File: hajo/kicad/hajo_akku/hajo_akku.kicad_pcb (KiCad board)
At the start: 2 copper layers, 62 x 92 mm, 21 parts, among them J1 Seetalk NG, J2 Debug, J3 Batteries, U1 MCP2562, U2 LF50CV, U3 WeMos_S2_mini

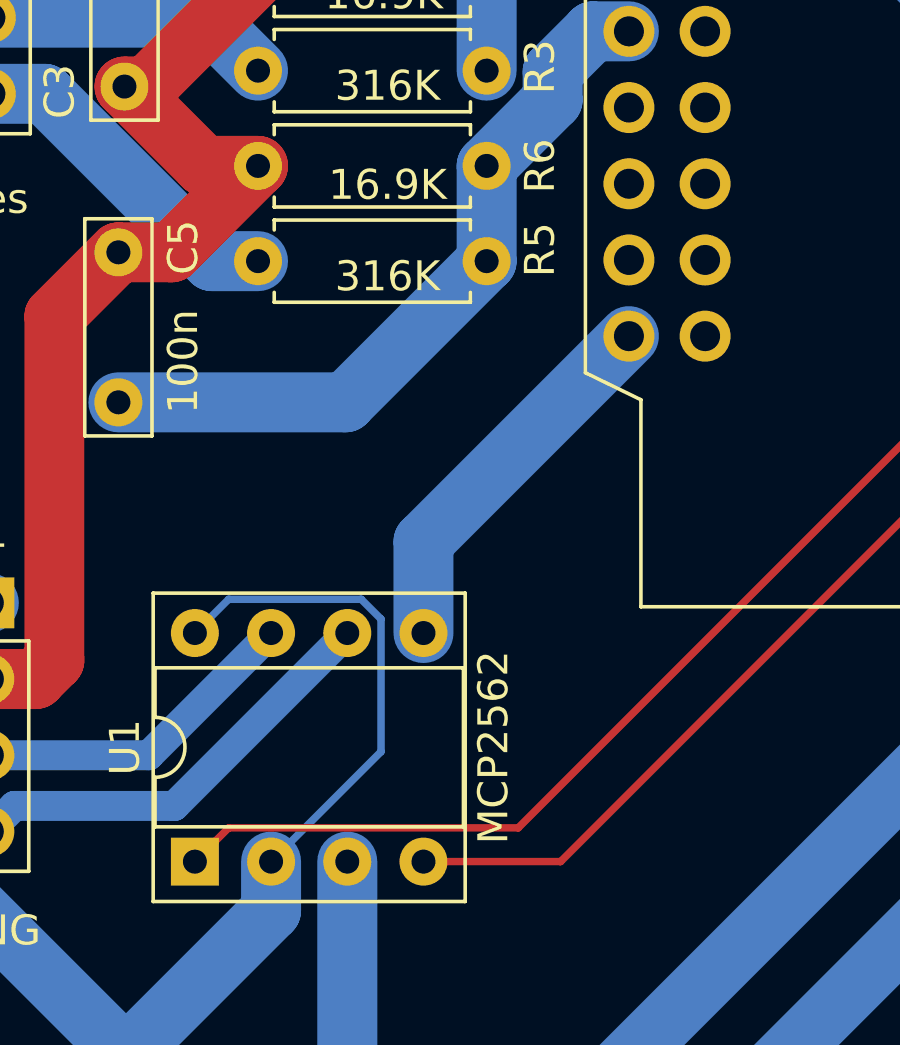
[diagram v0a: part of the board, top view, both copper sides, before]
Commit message: add back CanStby
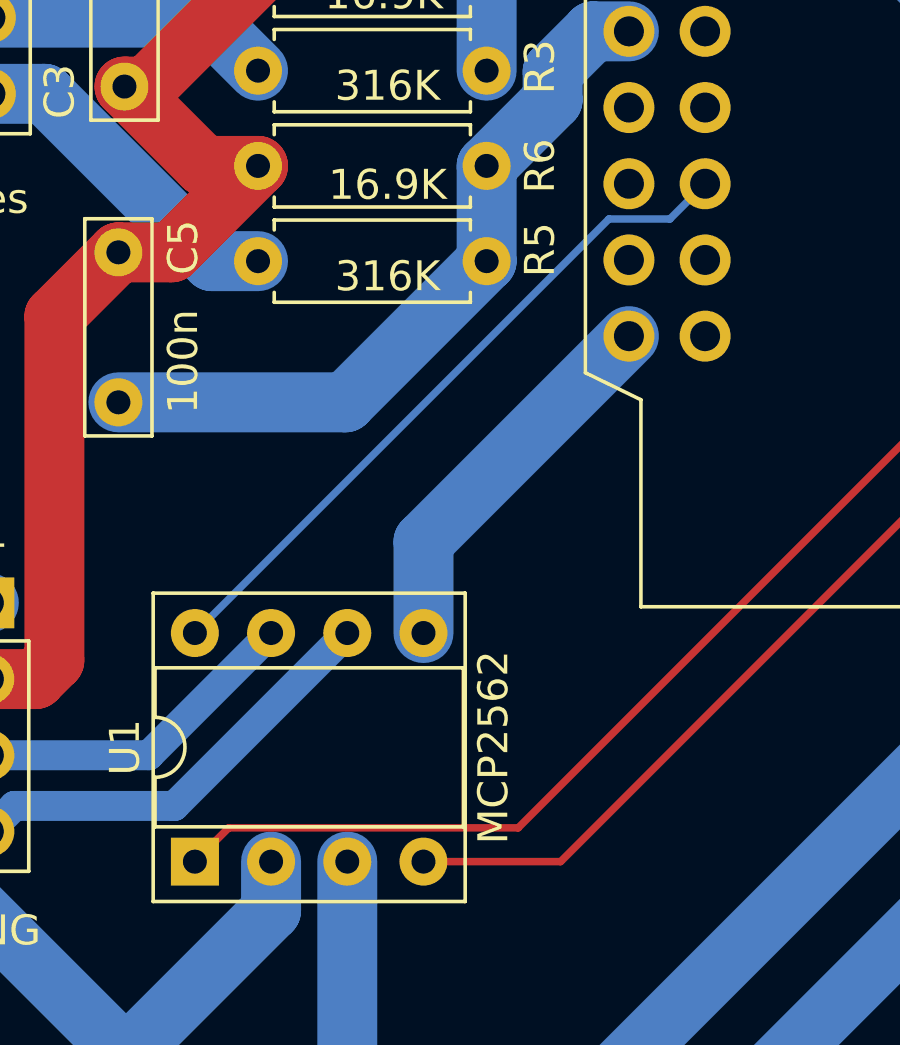
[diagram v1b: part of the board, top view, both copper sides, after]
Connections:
- net /RXD renamed /CanRx
- net /TXD renamed /CanTx
- U1 pad 8: GND -> /CanStby
- U3 pad 22: unconnected-(U3-GPIO10-Pad22) -> /CanStby
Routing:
- net /CanStby: track 0.00 -> 23.2 mm
- net GND: track 247.4 -> 230.9 mm
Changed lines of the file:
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@@
   (net 2 "/ADC2")
   (net 3 "/ADC3")
-  (net 4 "/TXD")
-  (net 5 "/RXD")
+  (net 4 "/CanTx")
+  (net 5 "/CanRx")
   (net 6 "unconnected-(U3-GPIO34-Pad29)")
   (net 7 "/CANH")
@@
   (net 17 "unconnected-(U3-GPIO33-Pad13)")
   (net 18 "unconnected-(U3-GPIO35-Pad14)")
-  (net 19 "unconnected-(U3-GPIO10-Pad22)")
+  (net 19 "/CanStby")
   (net 20 "unconnected-(U3-GPIO2-Pad18)")
   (net 21 "unconnected-(U3-GPIO4-Pad19)")
@@
       (net 23 "unconnected-(U3-GPIO8-Pad21)") (pinfunction "GPIO8") (pintype "bidirectional+no_connect"))
     (pad "22" thru_hole circle (at 2.54 12.7) (size 1.7 1.7) (drill 1) (layers "*.Cu" "*.Mask")
-      (net 19 "unconnected-(U3-GPIO10-Pad22)") (pinfunction "GPIO10") (pintype "bidirectional+no_connect"))
+      (net 19 "/CanStby") (pinfunction "GPIO10") (pintype "bidirectional"))
     (pad "23" thru_hole circle (at 2.54 15.24) (size 1.7 1.7) (drill 1) (layers "*.Cu" "*.Mask")
       (net 24 "unconnected-(U3-GPIO13-Pad23)") (pinfunction "GPIO13") (pintype "bidirectional+no_connect"))
@@
       (net 37 "unconnected-(U3-GPIO15-Pad25)") (pinfunction "GPIO15") (pintype "bidirectional+no_connect"))
     (pad "26" thru_hole circle (at 20.32 15.24) (size 1.7 1.7) (drill 1) (layers "*.Cu" "*.Mask")
-      (net 8 "GND") (pinfunction "GND") (pintype "passive"))
+      (net 8 "GND") (pinfunction "GND") (pintype "power_in"))
     (pad "27" thru_hole circle (at 20.32 12.7) (size 1.7 1.7) (drill 1) (layers "*.Cu" "*.Mask")
-      (net 5 "/RXD") (pinfunction "GPIO17") (pintype "bidirectional"))
+      (net 5 "/CanRx") (pinfunction "GPIO17") (pintype "bidirectional"))
     (pad "28" thru_hole circle (at 20.32 10.16) (size 1.7 1.7) (drill 1) (layers "*.Cu" "*.Mask")
-      (net 4 "/TXD") (pinfunction "GPIO21") (pintype "bidirectional"))
+      (net 4 "/CanTx") (pinfunction "GPIO21") (pintype "bidirectional"))
     (pad "29" thru_hole circle (at 20.32 7.62) (size 1.7 1.7) (drill 1) (layers "*.Cu" "*.Mask")
       (net 6 "unconnected-(U3-GPIO34-Pad29)") (pinfunction "GPIO34") (pintype "bidirectional+no_connect"))
@@
       (stroke (width 0.1) (type solid)) (layer "F.Fab"))
     (pad "1" thru_hole rect (at 0 0 90) (size 1.6 1.6) (drill 0.8) (layers "*.Cu" "*.Mask")
-      (net 4 "/TXD") (pinfunction "TXD") (pintype "input"))
+      (net 4 "/CanTx") (pinfunction "TXD") (pintype "input"))
     (pad "2" thru_hole oval (at 0 2.54 90) (size 1.6 1.6) (drill 0.8) (layers "*.Cu" "*.Mask")
       (net 8 "GND") (pinfunction "VSS") (pintype "power_in"))
@@
       (net 10 "+5V") (pinfunction "VDD") (pintype "power_in"))
     (pad "4" thru_hole oval (at 0 7.62 90) (size 1.6 1.6) (drill 0.8) (layers "*.Cu" "*.Mask")
-      (net 5 "/RXD") (pinfunction "RXD") (pintype "output"))
+      (net 5 "/CanRx") (pinfunction "RXD") (pintype "output"))
     (pad "5" thru_hole oval (at 7.62 7.62 90) (size 1.6 1.6) (drill 0.8) (layers "*.Cu" "*.Mask")
       (net 12 "+3.3V") (pinfunction "Vio") (pintype "power_in"))
@@
       (net 7 "/CANH") (pinfunction "CANH") (pintype "bidirectional"))
     (pad "8" thru_hole oval (at 7.62 0 90) (size 1.6 1.6) (drill 0.8) (layers "*.Cu" "*.Mask")
-      (net 8 "GND") (pinfunction "STBY") (pintype "input"))
+      (net 19 "/CanStby") (pinfunction "STBY") (pintype "input"))
     (model "${KICAD6_3DMODEL_DIR}/Package_DIP.3dshapes/DIP-8_W7.62mm_Socket.wrl"
       (offset (xyz 0 0 0))
@@
   (segment (start 77.77 59.228) (end 78.972081 59.228) (width 2) (layer "B.Cu") (net 8))
   (segment (start 74.870862 59.228) (end 77.77 59.228) (width 2) (layer "B.Cu") (net 8))
-  (segment (start 40.442 71.664) (end 41.567 70.539) (width 0.25) (layer "B.Cu") (net 8))
-  (segment (start 41.567 70.539) (end 45.987991 70.539) (width 0.25) (layer "B.Cu") (net 8))
   (segment (start 79.97 65.918) (end 79.97 60.412) (width 2) (layer "B.Cu") (net 8))
   (segment (start 61.26 26.716) (end 61.26 25.446) (width 2) (layer "B.Cu") (net 8))
   (segment (start 78.972081 59.228) (end 80.31 57.890081) (width 2) (layer "B.Cu") (net 8))
-  (segment (start 46.647 71.198009) (end 46.647 75.619) (width 0.25) (layer "B.Cu") (net 8))
   (segment (start 38.146 99.094888) (end 35.606 101.634888) (width 2) (layer "B.Cu") (net 8))
   (segment (start 42.982 79.284) (end 42.982 80.913138) (width 2) (layer "B.Cu") (net 8))
@@
   (segment (start 40.432 99.896888) (end 45.991112 99.896888) (width 2) (layer "B.Cu") (net 8))
   (segment (start 78.586214 33.85) (end 68.394 33.85) (width 2) (layer "B.Cu") (net 8))
-  (segment (start 45.987991 70.539) (end 46.647 71.198009) (width 0.25) (layer "B.Cu") (net 8))
   (segment (start 42.982 80.913138) (end 38.146 85.749138) (width 2) (layer "B.Cu") (net 8))
   (segment (start 38.948 99.896888) (end 38.146 99.094888) (width 2) (layer "B.Cu") (net 8))
   (segment (start 38.146 85.749138) (end 38.146 92.967888) (width 2) (layer "B.Cu") (net 8))
-  (segment (start 46.647 75.619) (end 42.982 79.284) (width 0.25) (layer "B.Cu") (net 8))
   (segment (start 29.324 73.82873) (end 32.49473 70.658) (width 2) (layer "B.Cu") (net 9))
   (segment (start 29.324 86.685888) (end 29.324 73.82873) (width 2) (layer "B.Cu") (net 9))
@@
   (segment (start 48.062 68.616) (end 54.91 61.768) (width 2) (layer "B.Cu") (net 12))
   (segment (start 48.062 71.664) (end 48.062 68.616) (width 2) (layer "B.Cu") (net 12))
+  (segment (start 40.442 71.664) (end 54.243 57.863) (width 0.25) (layer "B.Cu") (net 19))
+  (segment (start 56.275 57.863) (end 57.45 56.688) (width 0.25) (layer "B.Cu") (net 19))
+  (segment (start 54.243 57.863) (end 56.275 57.863) (width 0.25) (layer "B.Cu") (net 19))
   (segment (start 33.6248 48.6108) (end 37.8412 44.3944) (width 2) (layer "B.Cu") (net 27))
   (segment (start 37.8412 44.3944) (end 42.5148 44.3944) (width 2) (layer "B.Cu") (net 27))

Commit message: fix fluid measurement
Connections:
- U3 pad 11: unconnected-(U3-GPIO16-Pad11) -> /CanRx
- U3 pad 27: /CanRx -> /CanTx
- U3 pad 28: /CanTx -> unconnected-(U3-GPIO21-Pad28)
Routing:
- net /CanRx: track 36.5 -> 39.1 mm
- net /CanTx: track 45.2 -> 44.1 mm
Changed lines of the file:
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@@
   (net 32 "Net-(J3-Pin_2)")
   (net 33 "Net-(J3-Pin_3)")
-  (net 34 "unconnected-(U3-GPIO16-Pad11)")
+  (net 34 "unconnected-(U3-GPIO21-Pad28)")
   (net 35 "/DebugTX")
   (net 36 "/DebugRX")
@@
       (net 8 "GND") (pinfunction "GND") (pintype "power_in"))
     (pad "11" thru_hole circle (at 22.86 12.7) (size 1.7 1.7) (drill 1) (layers "*.Cu" "*.Mask")
-      (net 34 "unconnected-(U3-GPIO16-Pad11)") (pinfunction "GPIO16") (pintype "bidirectional+no_connect"))
+      (net 5 "/CanRx") (pinfunction "GPIO16") (pintype "bidirectional"))
     (pad "12" thru_hole circle (at 22.86 10.16) (size 1.7 1.7) (drill 1) (layers "*.Cu" "*.Mask")
       (net 31 "unconnected-(U3-GPIO18-Pad12)") (pinfunction "GPIO18") (pintype "bidirectional+no_connect"))
@@
       (net 37 "unconnected-(U3-GPIO15-Pad25)") (pinfunction "GPIO15") (pintype "bidirectional+no_connect"))
     (pad "26" thru_hole circle (at 20.32 15.24) (size 1.7 1.7) (drill 1) (layers "*.Cu" "*.Mask")
-      (net 8 "GND") (pinfunction "GND") (pintype "power_in"))
+      (net 8 "GND") (pinfunction "GND") (pintype "passive"))
     (pad "27" thru_hole circle (at 20.32 12.7) (size 1.7 1.7) (drill 1) (layers "*.Cu" "*.Mask")
-      (net 5 "/CanRx") (pinfunction "GPIO17") (pintype "bidirectional"))
+      (net 4 "/CanTx") (pinfunction "GPIO17") (pintype "bidirectional"))
     (pad "28" thru_hole circle (at 20.32 10.16) (size 1.7 1.7) (drill 1) (layers "*.Cu" "*.Mask")
-      (net 4 "/CanTx") (pinfunction "GPIO21") (pintype "bidirectional"))
+      (net 34 "unconnected-(U3-GPIO21-Pad28)") (pinfunction "GPIO21") (pintype "bidirectional+no_connect"))
     (pad "29" thru_hole circle (at 20.32 7.62) (size 1.7 1.7) (drill 1) (layers "*.Cu" "*.Mask")
       (net 6 "unconnected-(U3-GPIO34-Pad29)") (pinfunction "GPIO34") (pintype "bidirectional+no_connect"))
@@
   (segment (start 50.167 59.268) (end 50.167 56.093) (width 2) (layer "B.Cu") (net 3))
   (segment (start 52.367 52.948919) (end 52.367 53.893) (width 2) (layer "B.Cu") (net 3))
-  (segment (start 51.219 78.159) (end 75.23 54.148) (width 0.25) (layer "F.Cu") (net 4))
-  (segment (start 40.442 79.284) (end 41.567 78.159) (width 0.25) (layer "F.Cu") (net 4))
-  (segment (start 41.567 78.159) (end 51.219 78.159) (width 0.25) (layer "F.Cu") (net 4))
-  (segment (start 52.634 79.284) (end 75.23 56.688) (width 0.25) (layer "F.Cu") (net 5))
-  (segment (start 48.062 79.284) (end 52.634 79.284) (width 0.25) (layer "F.Cu") (net 5))
+  (segment (start 43.925198 75.800802) (end 40.442 79.284) (width 0.25) (layer "B.Cu") (net 4))
+  (segment (start 75.23 56.688) (end 70.021604 56.688) (width 0.25) (layer "B.Cu") (net 4))
+  (segment (start 70.021604 56.688) (end 50.908802 75.800802) (width 0.25) (layer "B.Cu") (net 4))
+  (segment (start 50.908802 75.800802) (end 43.925198 75.800802) (width 0.25) (layer "B.Cu") (net 4))
+  (segment (start 76.555 57.903) (end 69.443 57.903) (width 0.25) (layer "B.Cu") (net 5))
+  (segment (start 69.443 57.903) (end 48.062 79.284) (width 0.25) (layer "B.Cu") (net 5))
+  (segment (start 77.77 56.688) (end 76.555 57.903) (width 0.25) (layer "B.Cu") (net 5))
   (segment (start 38.908 75.738) (end 42.982 71.664) (width 1) (layer "B.Cu") (net 7))
   (segment (start 33.574 75.738) (end 38.908 75.738) (width 1) (layer "B.Cu") (net 7))
@@
   (segment (start 33.574 73.198) (end 35.134 73.198) (width 2) (layer "F.Cu") (net 8))
   (segment (start 38.0952 53.4476) (end 38.8424 53.4476) (width 2) (layer "F.Cu") (net 8))
+  (segment (start 57.45 43.988) (end 72.69 59.228) (width 0.25) (layer "F.Cu") (net 8))
   (segment (start 35.134 73.198) (end 35.7584 72.5736) (width 2) (layer "F.Cu") (net 8))
+  (segment (start 72.69 59.228) (end 75.23 59.228) (width 0.25) (layer "F.Cu") (net 8))
   (segment (start 40.7406 56.093) (end 38.0952 53.4476) (width 2) (layer "F.Cu") (net 8))
   (segment (start 38.2984 40.9362) (end 42.34 40.9362) (width 2) (layer "F.Cu") (net 8))
@@
   (segment (start 68.394 33.85) (end 61.26 26.716) (width 2) (layer "B.Cu") (net 8))
   (segment (start 31.524 74.74) (end 33.066 73.198) (width 2) (layer "B.Cu") (net 8))
-  (segment (start 57.45 43.988) (end 72.69 59.228) (width 0.25) (layer "B.Cu") (net 8))
   (segment (start 79.97 60.412) (end 78.786 59.228) (width 2) (layer "B.Cu") (net 8))
   (segment (start 33.066 73.198) (end 33.574 73.198) (width 2) (layer "B.Cu") (net 8))
@@
   (segment (start 45.991112 99.896888) (end 79.97 65.918) (width 2) (layer "B.Cu") (net 8))
   (segment (start 80.31 57.890081) (end 80.31 35.573786) (width 2) (layer "B.Cu") (net 8))
-  (segment (start 72.69 59.228) (end 75.23 59.228) (width 0.25) (layer "B.Cu") (net 8))
   (segment (start 40.432 99.896888) (end 45.991112 99.896888) (width 2) (layer "B.Cu") (net 8))
   (segment (start 78.586214 33.85) (end 68.394 33.85) (width 2) (layer "B.Cu") (net 8))

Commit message: amend & upgrade pcbs
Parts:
- added C6: 100n, Capacitor_THT:C_Rect_L7.0mm_W2.0mm_P5.00mm, F.Cu at (50.3, 96.9)
- added C7: 2.2u, Capacitor_THT:CP_Radial_D5.0mm_P2.00mm, F.Cu at (55.4, 97.6)
- added U4: LF33, Package_TO_SOT_THT:TO-220-3_Vertical, F.Cu at (50.3, 92.8)
- U1: footprint Package_DIP:DIP-8_W7.62mm_Socket -> Package_DIP:DIP-8_W7.62mm
- U2: value LF50CV -> LF50
- U3: footprint own:WEMOS_S2_mini_traced -> own:WEMOS_S2_mini
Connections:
- J2 pad 2: unconnected-(J2-Pin_2-Pad2) -> GND
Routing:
- net +3.3V: track 12.7 -> 48.6 mm
- net GND: track 230.9 -> 243.8 mm
- net +5V: track 71.2 -> 76.7 mm
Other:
- board text removed: "NC"

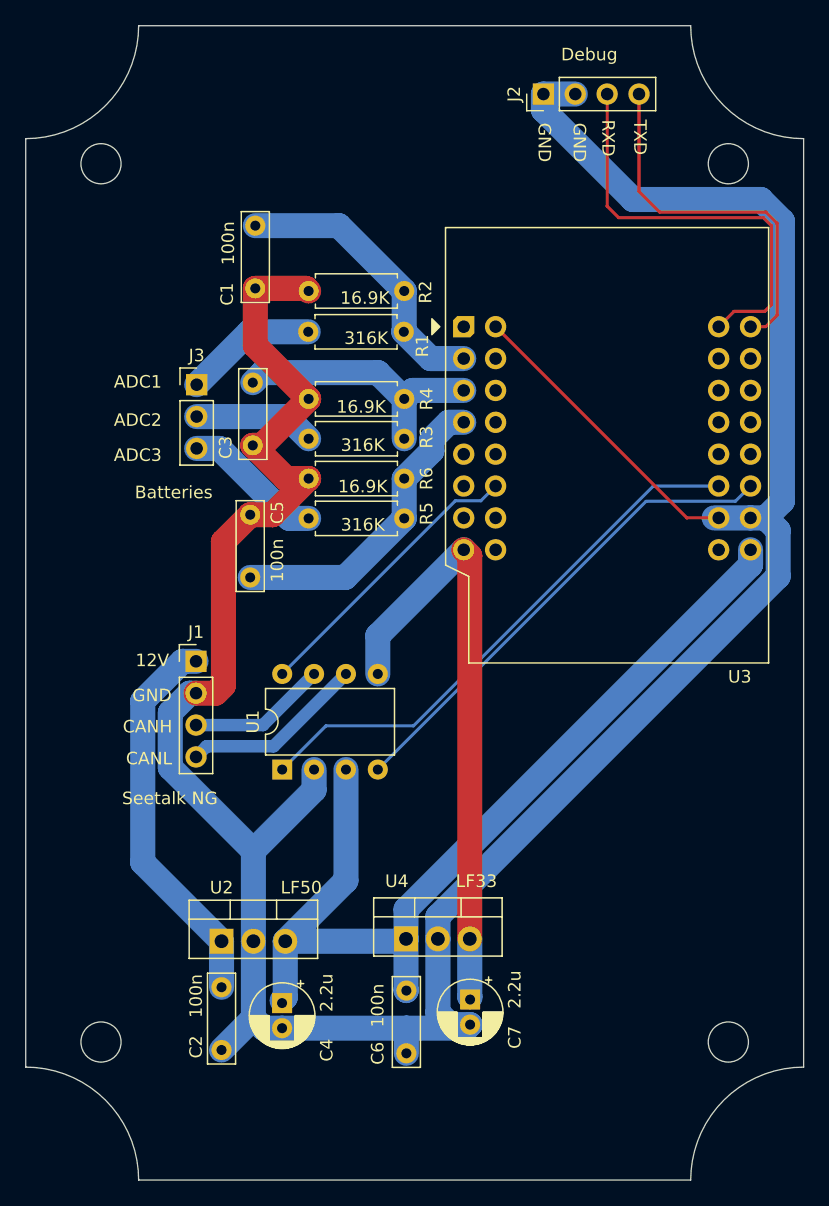
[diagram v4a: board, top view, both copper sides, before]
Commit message: update existing pcbs
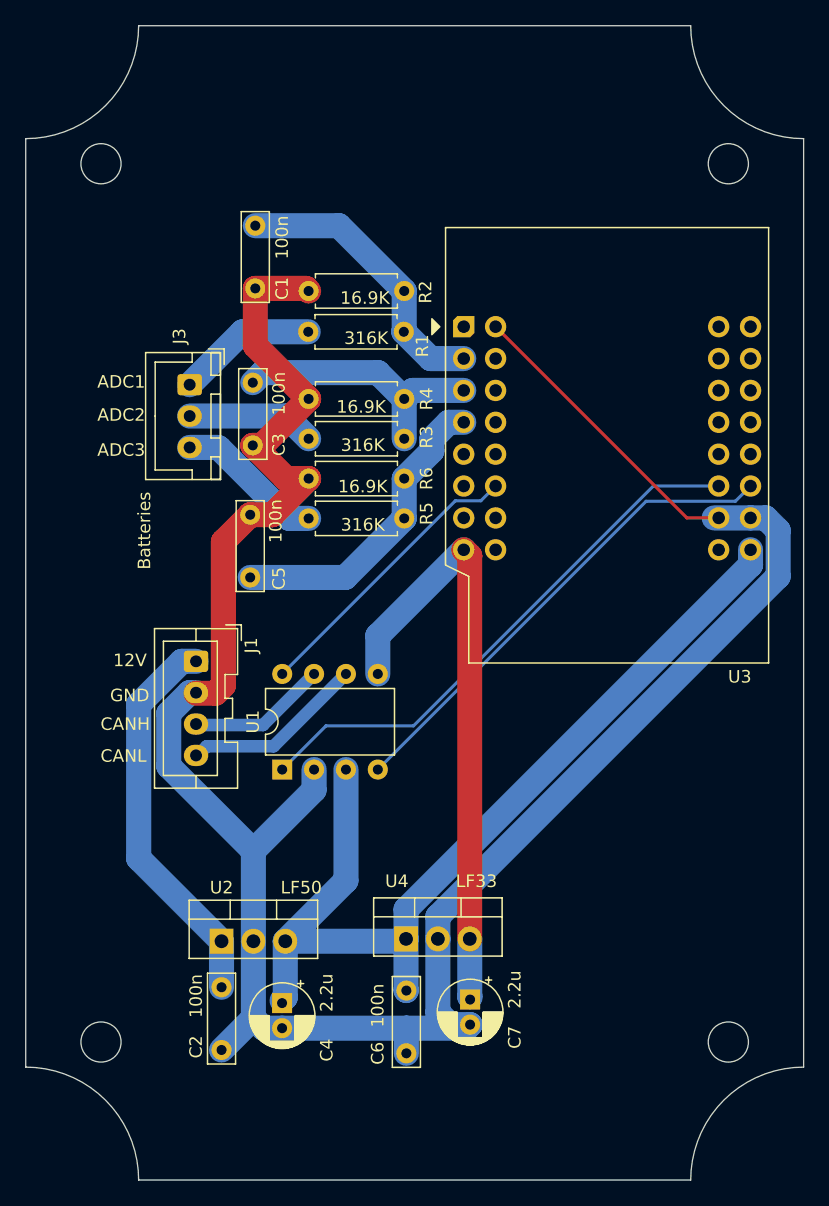
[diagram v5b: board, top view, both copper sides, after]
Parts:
- removed J2: Debug, Connector_PinHeader_2.54mm:PinHeader_1x04_P2.54mm_Vertical
- J1: footprint Connector_PinHeader_2.54mm:PinHeader_1x04_P2.54mm_Vertical -> Connector_JST:JST_XA_B04B-XASK-1_1x04_P2.50mm_Vertical
- J3: footprint Connector_PinHeader_2.54mm:PinHeader_1x03_P2.54mm_Vertical -> Connector_JST:JST_XH_B3B-XH-A_1x03_P2.50mm_Vertical
- moved J3 0.56 mm to (33.1, 48.6), turned to -90 degrees
- turned J1 to -90 degrees
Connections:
- U3 pad 16: /DebugTX -> unconnected-(U3-GPIO39-Pad16)
- U3 pad 32: /DebugRX -> unconnected-(U3-GPIO40-Pad32)
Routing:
- net GND: track 243.8 -> 193.2 mm
- net /DebugRX: track 33.9 -> 0.00 mm
- net /DebugTX: track 29.6 -> 0.00 mm
- net Net-(J3-Pin_3): track 11.2 -> 11.8 mm
- net Net-(J3-Pin_2): track 9.65 -> 10.2 mm
- net Net-(J3-Pin_1): track 10.6 -> 11.2 mm
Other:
- board text removed: "RXD"
- board text removed: "TXD"

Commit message: redesign akku pcb
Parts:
- removed C2, C6: 100n, Capacitor_THT:C_Rect_L7.0mm_W2.0mm_P5.00mm
- moved U4 15.3 mm to (57.6, 106.2), turned to 90 degrees
- moved U1 15.2 mm to (52.5, 88.6)
- moved J1 14.1 mm to (41.1, 82.6)
- moved C4 11.3 mm to (33.8, 107.1), turned to 90 degrees
- moved U2 9.29 mm to (40.1, 101.1), turned to -90 degrees
- moved C3 9.03 mm to (43.9, 46.5), turned to 0 degrees
- moved C7 8.18 mm to (63.2, 100.3)
- moved C1 7.65 mm to (43.5, 35.4), turned to 0 degrees
- moved C5 6.31 mm to (44.2, 58.2), turned to 0 degrees
- moved R5 5.17 mm to (50.2, 64.4)
- moved R6 5.17 mm to (42.6, 61.3)
- moved J3 3.81 mm to (36.9, 48.7)
- moved R1 2.44 mm to (49.8, 42.0)
- moved R2 2.44 mm to (42.2, 38.7)
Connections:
- J1 pad 2: GND -> /CANH
- J1 pad 3: /CANH -> /CANL
- J1 pad 4: /CANL -> GND
- U1 pad 8: /CanStby -> GND
- U3 pad 22: /CanStby -> unconnected-(U3-GPIO10-Pad22)
- U3 pad 9: +5V -> unconnected-(U3-VBUS-Pad9)
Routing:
- net GND: track 193.2 -> 222.4 mm
- net /CanStby: track 23.2 -> 0.00 mm
- net +5V: track 76.7 -> 54.6 mm
- net +3.3V: track 48.6 -> 62.7 mm
- net +12V: track 31.3 -> 20.7 mm
- net /ADC2: track 21.5 -> 11.9 mm
- net /ADC1: track 22.9 -> 14.2 mm
- net /ADC3: track 24.6 -> 15.9 mm
- net /CANH: track 11.1 -> 15.7 mm
- net /CANL: track 14.7 -> 19.3 mm
- net Net-(J3-Pin_2): track 10.2 -> 6.37 mm
- net Net-(J3-Pin_1): track 11.2 -> 8.93 mm
- net Net-(J3-Pin_3): track 11.8 -> 13.1 mm
- net /CanRx: track 39.1 -> 40.3 mm
- net /CanTx: track 44.1 -> 45.1 mm
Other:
- outline, holes or cut-outs redrawn
